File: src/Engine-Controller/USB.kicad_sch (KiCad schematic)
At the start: 8 parts, among them P2 USB, U7 CP2102-GMR(QFN28)

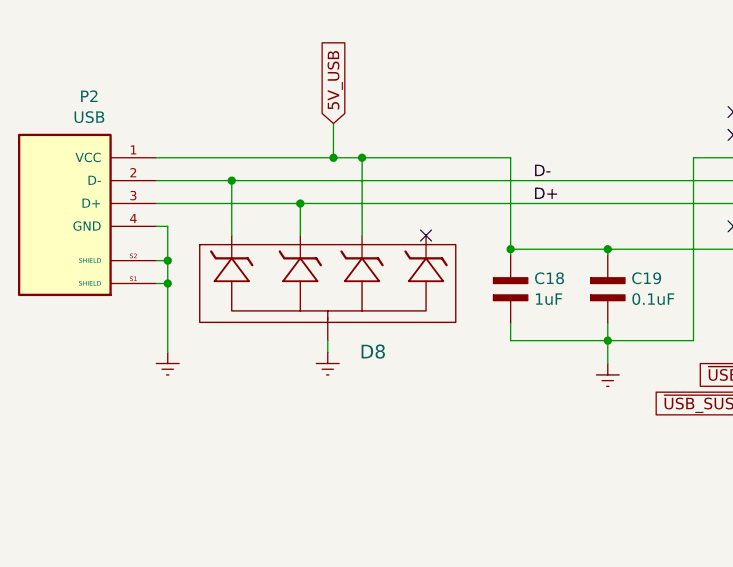
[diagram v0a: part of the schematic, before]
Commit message: Removed misc elements from connectors sheet
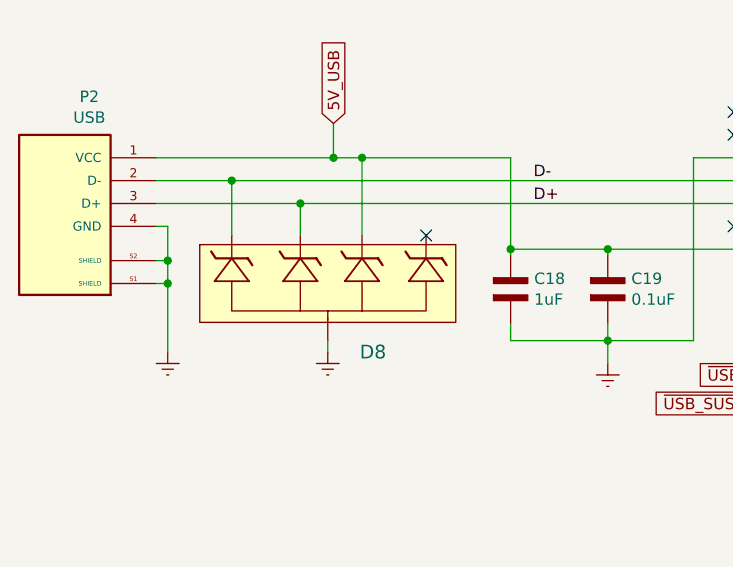
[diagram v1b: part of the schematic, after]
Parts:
- D8: footprint Engine-Controller:SP0504BAHTG -> SOD-123FL_MCC
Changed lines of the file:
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@@
       (effects (font (size 1.524 1.524)) hide)
     )
-    (property "Footprint" "Engine-Controller:SP0504BAHTG" (id 2) (at 95.377 105.791 0)
+    (property "Footprint" "SOD-123FL_MCC" (id 2) (at 95.377 105.791 0)
       (effects (font (size 1.524 1.524)) hide)
     )
